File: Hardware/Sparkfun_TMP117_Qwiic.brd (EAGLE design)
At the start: 25.4 x 25.4 mm, 43 parts, among them J1 PTH, U2 TMP117

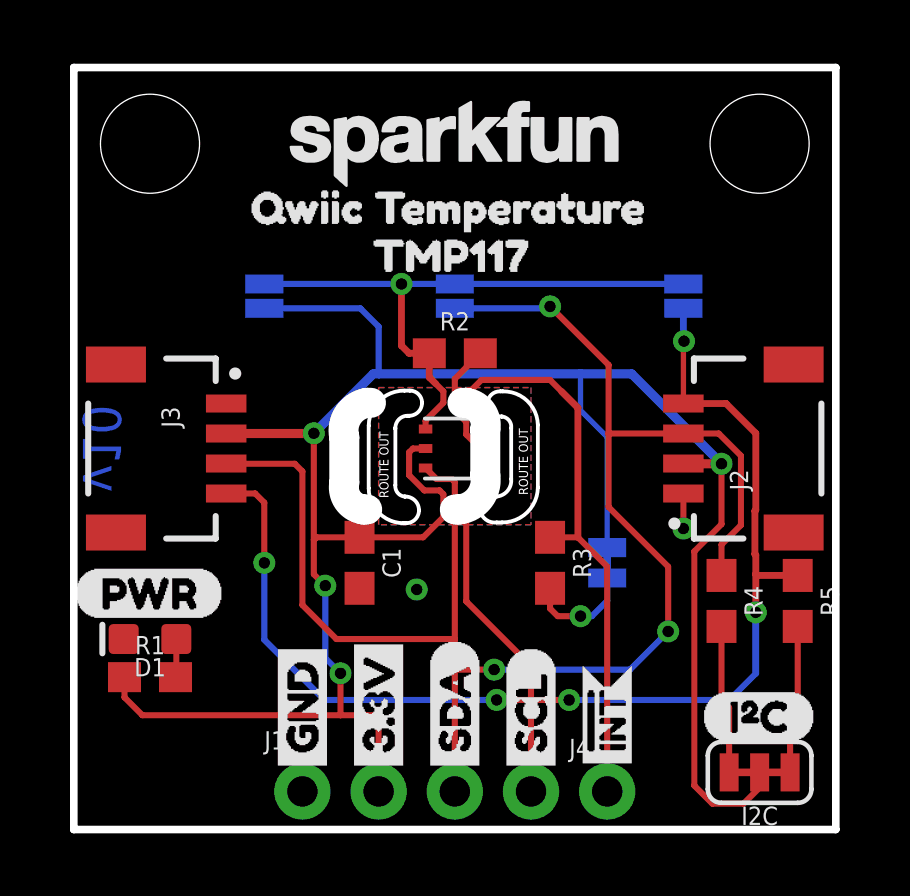
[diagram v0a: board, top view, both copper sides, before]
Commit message: more layout changes
-moved to 4 jumpers on address select, to fully remove pull resisor when you cut trace. Previous version had pull down resistor permenantly in circuit, so it would be tied to SDA or SCL when those address options were selected.
-SCH cleanup
-rerouting as necessary.
-added LED bypass jumper
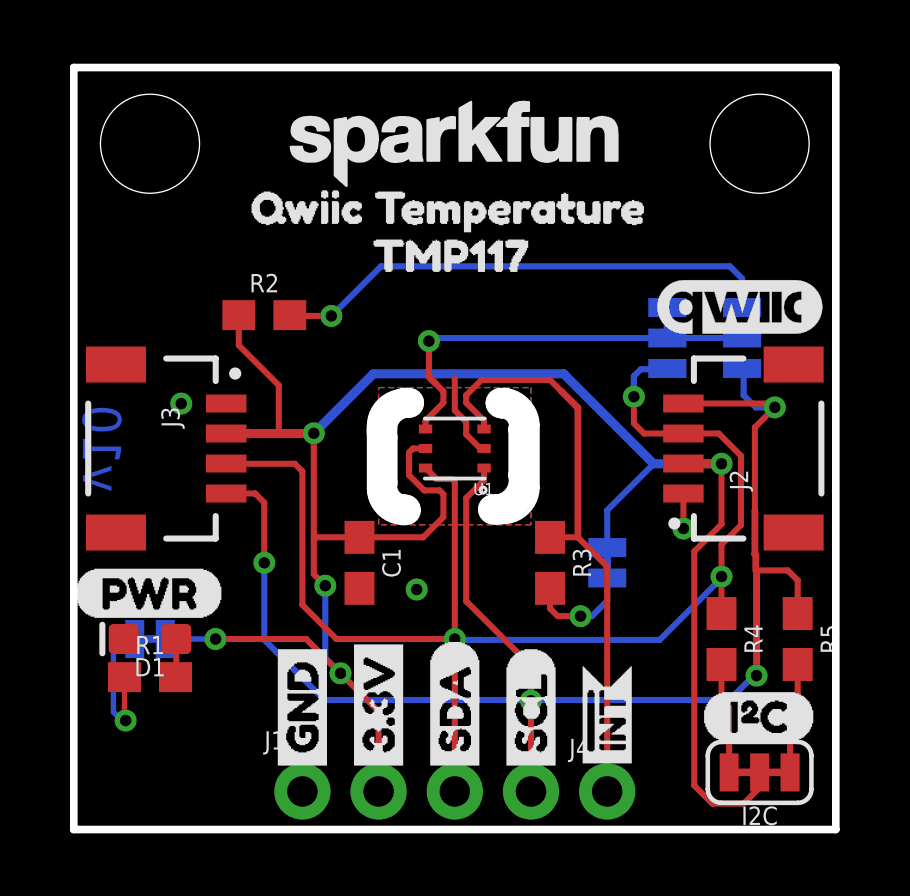
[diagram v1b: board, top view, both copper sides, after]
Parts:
- removed JP2, JP3: (no value), SparkFun-Jumpers:SMT-JUMPER_2_NO_SILK
- removed U$18: (no value), buzzard_labels (15):ADR_#_0X484
- removed U$8: (no value), buzzard_labels (15):0X493
- added JP4: JUMPER-SMT_3_1-NC_TRACE_NO-SILK, SparkFun-Jumpers:SMT-JUMPER_3_1-NC_TRACE_NO-SILK
- added JP5: JUMPER-SMT_3_NO_NO_SILK, SparkFun-Jumpers:SMT-JUMPER_3_0-NO_TRACE_NO-SILK
- added U$16: (no value), buzzard_labels (25):0X4A2
- added U$17: (no value), buzzard_labels (25):0X4B3
- added U$2: (no value), buzzard_labels (25):0X491
- added U$42: (no value), buzzard_labels (26):0X480
- added U$45: (no value), buzzard_labels (22):ADDR0
- J2, J3: value (none) -> Qwiic
- JP1: value (none) -> LED; device SparkFun-Jumpers:SMT-JUMPER_2_NO_SILK -> SparkFun-Jumpers:SMT-JUMPER_2_NC_TRACE_SILK
- U$1: device buzzard_labels (15):0X4B1 -> buzzard_labels (2):QWIIC_TEMPERATURE2
- U$5: device buzzard_labels (15):0X4A0 -> buzzard_labels:TMP1171
- moved JP1 21.1 mm to (2.54, 6.35), turned to 180 degrees
- moved U$15 20.5 mm to (22.2, 17.4), flipped to the top
- moved LOGO1 20.3 mm to (22.9, 2.54)
- moved R2 6.48 mm to (6.35, 17.1)
- moved U$1 5.98 mm to (19.9, 20.8)
- moved U$5 3.59 mm to (16.2, 19.1)
- moved U$7 2.54 mm to (22.4, 8.86)
- moved R4 1.27 mm to (21.6, 6.35)
- moved R5 1.27 mm to (24.1, 6.35)
- renumbered U2 to U1
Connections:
- new net N$7: JP5.1, R2.2
- new net N$8: JP1.1, R1.1
- net 3.3V: now also JP1.2, R2.1; no longer JP3.2, R1.1
- net ADD0: now also JP4.2, JP5.2; no longer JP1.1, JP2.1, JP3.1, R2.1
- net GND: now also JP4.3; no longer R2.2
- net SCL: now also JP5.3; no longer JP1.2
- net SDA: now also JP4.1; no longer JP2.2
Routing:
- net N$7: track 0.00 -> 16.9 mm, vias 0 -> 1
- net SDA: track 56.4 -> 46.3 mm
- net 3.3V: track 75.8 -> 69.4 mm, vias 4 -> 5
- net ADD0: track 20.0 -> 13.9 mm
- net N$8: track 0.00 -> 5.05 mm, vias 0 -> 1
- net SCL: track 50.9 -> 52.7 mm, vias 5 -> 4
- net N$2: track 4.97 -> 3.70 mm
- net N$3: track 4.97 -> 3.70 mm
- net GND: track 5.17 -> 3.97 mm, vias 2 -> 3
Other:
- outline, holes or cut-outs redrawn

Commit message: post design review changes
-Added fiducials
-added bottom two standoffs
-switched to SFE logo with flame
-moved I2C jumper to bottom
-added outer box silk to address jumpers
-moved pwr LED and jumper to make room for standoff
-changes all traces to 8 mil, except 3.3V power up to 16 mil.
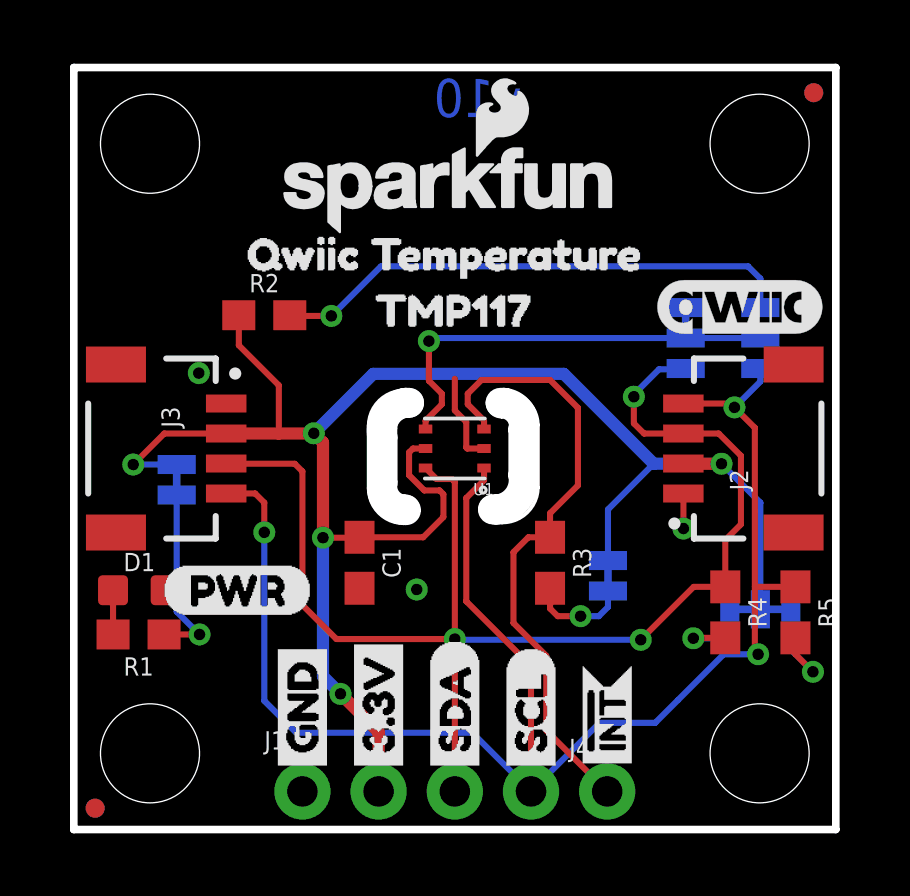
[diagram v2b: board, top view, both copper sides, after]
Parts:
- removed LOGO3: SFE_LOGO_NAME.1_INCH, SparkFun-Aesthetics:SFE_LOGO_NAME_.1
- removed U$45: (no value), buzzard_labels (22):ADDR0
- added FD1, FD2, FD3, FD4: FIDUCIALUFIDUCIAL, SparkFun-Aesthetics:FIDUCIAL-MICRO
- added JP2, JP3: STAND-OFF, SparkFun:STAND-OFF
- added LOGO4: SFE_LOGO_NAME_FLAME.1_INCH, SparkFun-Aesthetics:SFE_LOGO_NAME_FLAME_.1
- added U$18: (no value), buzzard_labels (1):ADDR0
- added U$8: (no value), buzzard_labels (5):LED0
- JP10: device SparkFun-Passives:PAD-JUMPER-2-NC_BY_TRACE_YES_SILK -> SparkFun-Jumpers:SMT-JUMPER_2_NC_TRACE_SILK
- LOGO2: value SFE_LOGO_NAME.1_INCH -> SFE_LOGO_NAME_FLAME.1_INCH; device SparkFun-Aesthetics:SFE_LOGO_NAME_.1 -> SparkFun-Aesthetics:SFE_LOGO_NAME_FLAME_.1
- moved LOGO1 26.2 mm to (2.54, 19.1)
- moved U$21 6.59 mm to (24.8, 9.12), flipped to the bottom
- moved I2C 5.44 mm to (22.9, 7.34), flipped to the bottom, turned to 0 degrees
- moved JP1 5.38 mm to (3.43, 11.7), turned to 90 degrees
- moved U$20 2.95 mm to (2.95, 7.98)
- moved U$7 2.91 mm to (19.9, 10.4)
- moved U$4 1.83 mm to (9.14, 17.3)
- moved U$5 1.83 mm to (16.2, 17.3)
- moved D1 1.66 mm to (2.18, 7.98), turned to 0 degrees
- moved U$1 1.60 mm to (19.9, 19.2)
- moved U$6 1.55 mm to (4.88, 19.2)
- moved LOGO2 1.53 mm to (12.5, 21.3), flipped to the bottom
- moved R1 1.47 mm to (2.16, 6.50), turned to 180 degrees
- moved R4 0.90 mm to (21.7, 7.24)
- moved R5 0.89 mm to (24.1, 7.24)
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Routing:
- net 3.3V: track 69.4 -> 59.2 mm
- net !INT: track 19.8 -> 21.0 mm
- net N$8: track 5.05 -> 6.15 mm
- net SDA: track 46.3 -> 45.5 mm
- net N$7: track 16.9 -> 17.5 mm
- net ADD0: track 13.9 -> 14.4 mm
- net N$3: track 3.70 -> 3.20 mm, vias 0 -> 1
- net SCL: track 52.7 -> 52.8 mm, vias 4 -> 3
- net N$2: track 3.70 -> 3.76 mm, vias 0 -> 1
- removed copper zone on layer 16, net N$5
- removed copper zone on layer 1, net N$6

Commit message: parts to SFE libraries
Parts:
- J1: device SparkX:1X04_NO_SILK -> SparkFun-Connectors:1X04_NO_SILK
- J2, J3: value Qwiic -> QWIIC_RA
- U1: device TMP117:TMP117 -> SparkFun-Sensors:TMP117
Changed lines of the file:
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@@
 </element>
 <element name="FRAME1" library="SparkFun-Aesthetics" library_urn="urn:adsk.eagle:library:507" package="CREATIVE_COMMONS" package3d_urn="urn:adsk.eagle:package:37121/1" value="FRAME-LETTER" x="-7.62" y="-8.89" smashed="yes"/>
-<element name="J1" library="SparkX" package="1X04_NO_SILK" value="PTH" x="7.62" y="1.27" smashed="yes">
+<element name="J1" library="SparkFun-Connectors" package="1X04_NO_SILK" value="PTH" x="7.62" y="1.27" smashed="yes">
 <attribute name="NAME" x="6.35" y="2.667" size="0.6096" layer="25" font="vector" ratio="20"/>
 <attribute name="VALUE" x="6.35" y="-0.762" size="0.6096" layer="27" font="vector" ratio="20"/>
 </element>
-<element name="J3" library="SparkFun-Connectors" package="JST04_1MM_RA" value="Qwiic" x="5.08" y="12.7" smashed="yes" rot="R270">
+<element name="J3" library="SparkFun-Connectors" package="JST04_1MM_RA" value="QWIIC_RA" x="5.08" y="12.7" smashed="yes" rot="R270">
 <attribute name="NAME" x="2.921" y="14.097" size="0.6096" layer="25" font="vector" ratio="20" rot="R270"/>
 <attribute name="PROD_ID" value="CONN-13694" x="-8.89" y="-3.81" size="1.778" layer="27" rot="R270" display="off"/>
-<attribute name="VALUE" x="1.778" y="14.351" size="0.6096" layer="27" font="vector" ratio="20" rot="R270"/>
+<attribute name="VALUE" value="QWIIC_RIGHT_ANGLE" x="1.778" y="14.351" size="0.6096" layer="27" font="vector" ratio="20" rot="R270"/>
 </element>
 <element name="J4" library="SparkFun-Connectors" package="1X01_NO_SILK" value="" x="17.78" y="1.27" smashed="yes">
@@
 <attribute name="VALUE" x="23.2918" y="7.239" size="0.6096" layer="27" font="vector" ratio="20" rot="R270" align="top-center"/>
 </element>
-<element name="J2" library="SparkFun-Connectors" package="JST04_1MM_RA" value="Qwiic" x="20.32" y="12.7" smashed="yes" rot="R90">
+<element name="J2" library="SparkFun-Connectors" package="JST04_1MM_RA" value="QWIIC_RA" x="20.32" y="12.7" smashed="yes" rot="R90">
 <attribute name="NAME" x="22.479" y="11.303" size="0.6096" layer="25" font="vector" ratio="20" rot="R90"/>
 <attribute name="PROD_ID" value="CONN-13694" x="19.05" y="12.7" size="1.778" layer="27" ratio="15" rot="R90" display="off"/>
-<attribute name="VALUE" x="23.622" y="11.049" size="0.6096" layer="27" font="vector" ratio="20" rot="R90"/>
+<attribute name="VALUE" value="QWIIC_RIGHT_ANGLE" x="23.622" y="11.049" size="0.6096" layer="27" font="vector" ratio="20" rot="R90"/>
 </element>
 <element name="JP8" library="SparkFun" package="STAND-OFF" value="STAND-OFF" x="22.86" y="22.86" smashed="yes"/>
@@
 <element name="U$13" library="Labels" package="SDA-[)" value="" x="12.7" y="1.651" smashed="yes" rot="R90"/>
 <element name="U$14" library="Labels" package="SDA-[)" value="" x="12.7" y="1.651" smashed="yes" rot="MR90"/>
-<element name="U1" library="TMP117" package="TMP117" value="TMP117" x="12.7" y="12.7" smashed="yes" rot="R180">
+<element name="U1" library="SparkFun-Sensors" package="TMP117" value="TMP117" x="12.7" y="12.7" smashed="yes" rot="R180">
 <attribute name="NAME" x="14" y="11.55" size="0.4064" layer="25" rot="R180"/>
+<attribute name="PROD_ID" value="IC-14700" x="12.7" y="12.7" size="1.778" layer="27" rot="R180" display="off"/>
 <attribute name="VALUE" x="14" y="14.2" size="0.4064" layer="27" rot="R180"/>
 </element>
